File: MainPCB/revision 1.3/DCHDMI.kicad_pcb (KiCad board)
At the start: 4 copper layers, 66.6 x 51.3 mm, 105 parts, among them CON1 3-1775333-2, CON2 DC2R019JA7R1700, CON3 CONN_01X06, CON4 CONN_01X03, CON5 CONN_01X03, SW1 SW_DIP_x02, U1 MCP1826S-1202E/DB, U2 MIC5219-2.5YM5-TR, U3 LP5907MFX-1.8/NOPB, U4 ADV7513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

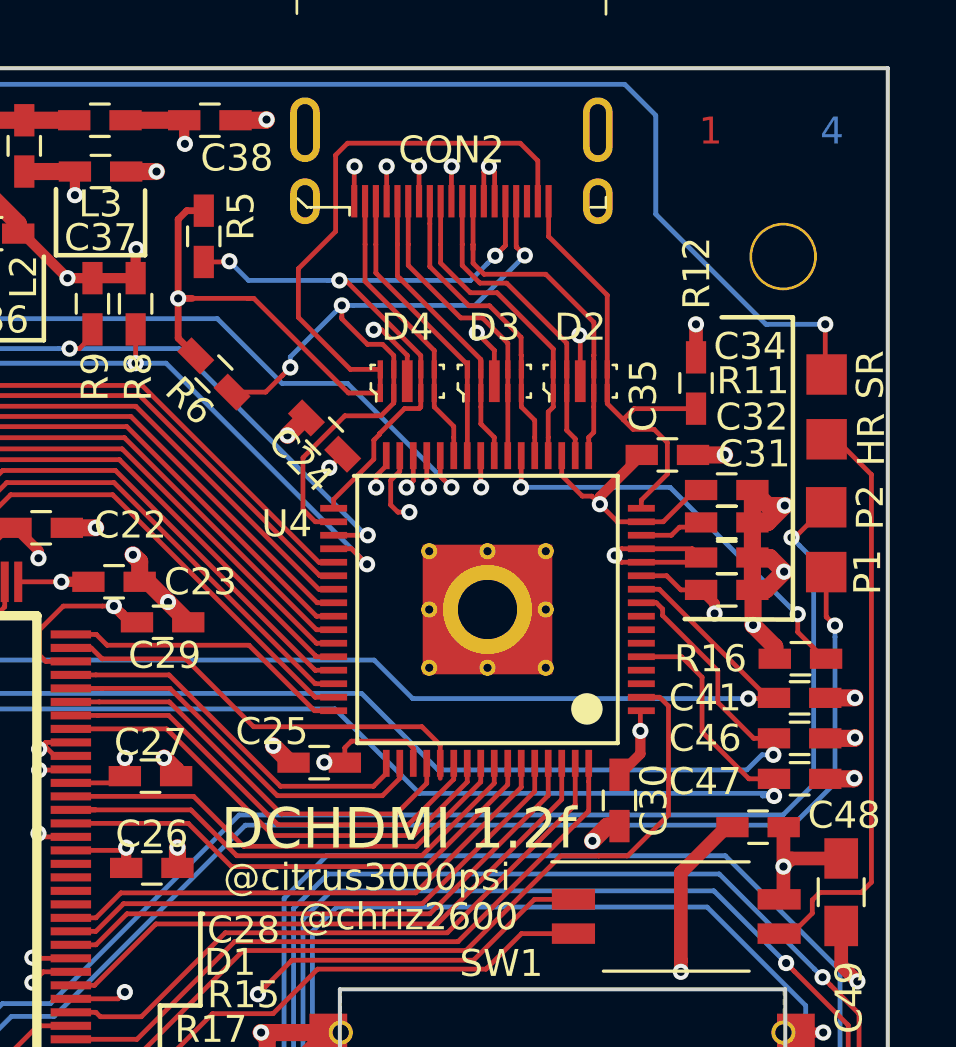
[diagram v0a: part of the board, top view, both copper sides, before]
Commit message: Added 470 series resistor
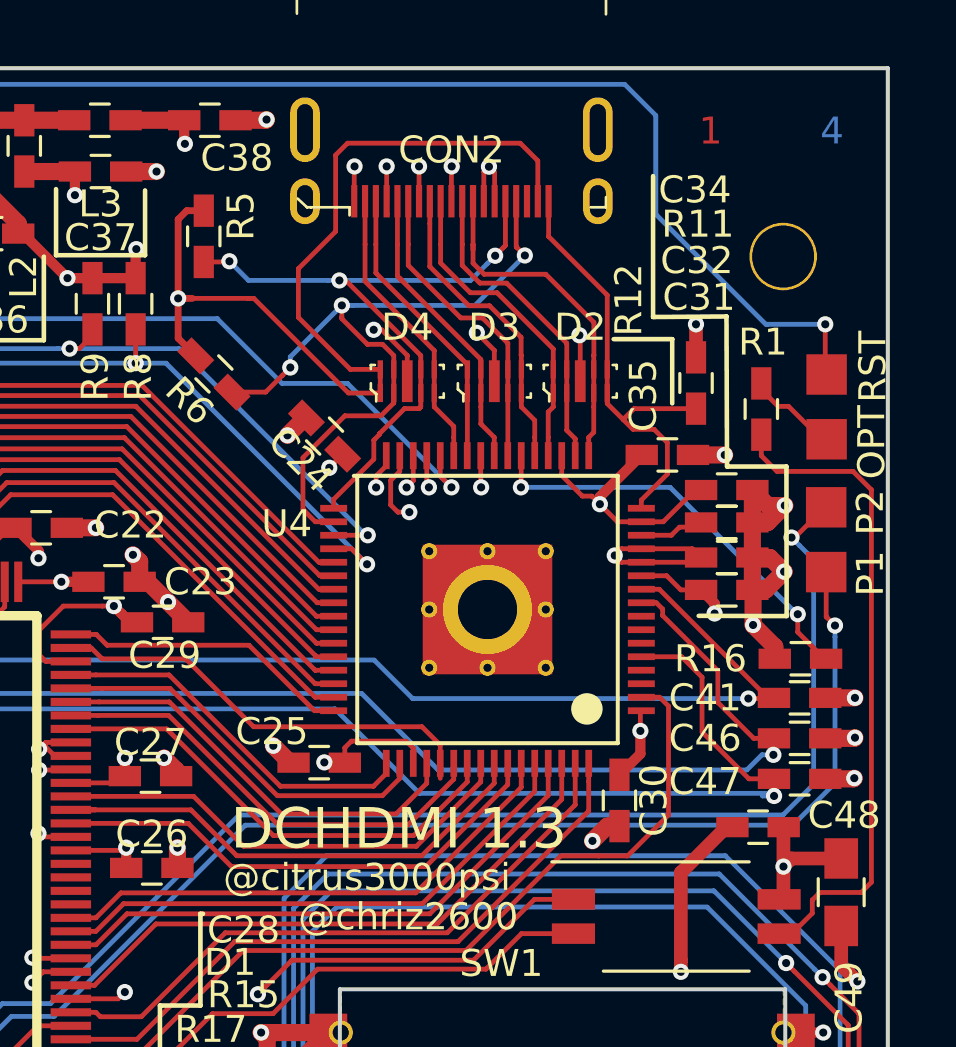
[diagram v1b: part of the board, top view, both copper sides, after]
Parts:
- added R1: 470, Capacitors_SMD:C_0603_HandSoldering, F.Cu at (183.9, 86.3)
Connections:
- SW1 pad 3: /HRST_OUT -> Net-(R1-Pad2)
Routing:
- net Net-(R1-Pad2): track 0.00 -> 24.8 mm
- net /HRST_OUT: track 22.2 -> 3.76 mm
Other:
- board text added: "DCHDMI 1.3"
- board text added: "OPT"
- board text added: "RST"
- board text removed: "DCHDMI 1.2f"
- board text removed: "HR"
- board text removed: "SR"
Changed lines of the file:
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@@
   (general
     (thickness 1.6)
-    (drawings 63)
-    (tracks 1976)
+    (drawings 68)
+    (tracks 1984)
     (zones 0)
-    (modules 105)
-    (nets 130)
+    (modules 106)
+    (nets 131)
   )
   (page A4)
@@
   (net 128 "Net-(U6-Pad22)")
   (net 129 "Net-(U8-Pad1)")
+  (net 130 "Net-(R1-Pad2)")
   (net_class Default "This is the default net class."
     (clearance 0.15)
@@
     (add_net "Net-(CON3-Pad6)")
     (add_net "Net-(D1-Pad1)")
+    (add_net "Net-(R1-Pad2)")
     (add_net "Net-(R11-Pad1)")
     (add_net "Net-(R14-Pad1)")
@@
     (tags "capacitor 0603")
     (attr smd)
-    (fp_text reference C31 (at 1.01 -5.04) (layer F.SilkS)
+    (fp_text reference C31 (at -1.03 -10.84) (layer F.SilkS)
       (effects (font (size 1 1) (thickness 0.15)))
     )
@@
       (effects (font (size 0.2 0.2) (thickness 0.05)))
     )
-    (fp_text user %R (at 1.01 -5.03) (layer F.Fab)
+    (fp_text user %R (at -1.03 -10.83) (layer F.Fab)
       (effects (font (size 1 1) (thickness 0.15)))
     )
@@
     (tags "capacitor 0603")
     (attr smd)
-    (fp_text reference C32 (at 0.93 -5.2) (layer F.SilkS)
+    (fp_text reference C32 (at -1.11 -11) (layer F.SilkS)
       (effects (font (size 1 1) (thickness 0.15)))
     )
@@
       (effects (font (size 0.2 0.2) (thickness 0.05)))
     )
-    (fp_text user %R (at 0.93 -5.22) (layer F.Fab)
+    (fp_text user %R (at -1.11 -11.02) (layer F.Fab)
       (effects (font (size 1 1) (thickness 0.15)))
     )
@@
     (tags "capacitor 0603")
     (attr smd)
-    (fp_text reference C34 (at 0.86 -5.32) (layer F.SilkS)
+    (fp_text reference C34 (at -1.18 -11.12) (layer F.SilkS)
       (effects (font (size 1 1) (thickness 0.15)))
     )
@@
       (effects (font (size 0.2 0.2) (thickness 0.05)))
     )
-    (fp_text user %R (at 0.89 -5.36) (layer F.Fab)
+    (fp_text user %R (at -1.15 -11.16) (layer F.Fab)
       (effects (font (size 1 1) (thickness 0.15)))
     )
@@
     (tags "capacitor 0603")
     (attr smd)
-    (fp_text reference R11 (at 0.97 -5.25) (layer F.SilkS)
+    (fp_text reference R11 (at -1.07 -11.05) (layer F.SilkS)
       (effects (font (size 1 1) (thickness 0.15)))
     )
@@
       (effects (font (size 0.2 0.2) (thickness 0.05)))
     )
-    (fp_text user %R (at 0.97 -5.25) (layer F.Fab)
+    (fp_text user %R (at -1.07 -11.05) (layer F.Fab)
       (effects (font (size 1 1) (thickness 0.15)))
     )
@@
     (tags "capacitor 0603")
     (attr smd)
-    (fp_text reference R12 (at 4.0648 0.0282 90) (layer F.SilkS)
+    (fp_text reference R12 (at 3.0748 -2.4918 270) (layer F.SilkS)
       (effects (font (size 1 1) (thickness 0.15)))
     )
@@
       (effects (font (size 0.2 0.2) (thickness 0.05)))
     )
-    (fp_text user %R (at 4.0948 0.0482 90) (layer F.Fab)
+    (fp_text user %R (at 3.0848 -2.5118 90) (layer F.Fab)
       (effects (font (size 1 1) (thickness 0.15)))
     )
@@
       (net 113 /ESP_SCL))
     (pad 3 smd rect (at 3.81 0.635) (size 1.6 0.76) (layers F.Cu F.Mask)
-      (net 122 /HRST_OUT))
+      (net 130 "Net-(R1-Pad2)"))
     (pad 2 smd rect (at -3.81 0.635) (size 1.6 0.76) (layers F.Cu F.Mask)
       (net 123 /HRST))
@@
     )
   )
-  (gr_line (start 185.05 94.1) (end 181.04 94.08) (layer F.SilkS) (width 0.17))
-  (gr_line (start 185.05 82.9) (end 185.05 94.1) (layer F.SilkS) (width 0.17))
-  (gr_line (start 182.41 82.9) (end 185.05 82.9) (layer F.SilkS) (width 0.17))
-  (gr_text SR (at 187.92 85.03 90) (layer F.SilkS)
+  (module Capacitors_SMD:C_0603_HandSoldering (layer F.Cu)
+    (at 183.88 86.3 270)
+    (descr "Capacitor SMD 0603, hand soldering")
+    (tags "capacitor 0603")
+    (attr smd)
+    (fp_text reference R1 (at -2.48 -0.06) (layer F.SilkS)
+      (effects (font (size 1 1) (thickness 0.15)))
+    )
+    (fp_text value 470 (at -0.01 0) (layer F.Fab)
+      (effects (font (size 0.15 0.15) (thickness 0.0375)))
+    )
+    (fp_text user %R (at -2.48 -0.04) (layer F.Fab)
+      (effects (font (size 1 1) (thickness 0.15)))
+    )
+    (fp_line (start -0.8 0.4) (end -0.8 -0.4) (layer F.Fab) (width 0.1))
+    (fp_line (start 0.8 0.4) (end -0.8 0.4) (layer F.Fab) (width 0.1))
+    (fp_line (start 0.8 -0.4) (end 0.8 0.4) (layer F.Fab) (width 0.1))
+    (fp_line (start -0.8 -0.4) (end 0.8 -0.4) (layer F.Fab) (width 0.1))
+    (fp_line (start -0.35 -0.6) (end 0.35 -0.6) (layer F.SilkS) (width 0.12))
+    (fp_line (start 0.35 0.6) (end -0.35 0.6) (layer F.SilkS) (width 0.12))
+    (fp_line (start -1.8 -0.65) (end 1.8 -0.65) (layer F.CrtYd) (width 0.05))
+    (fp_line (start -1.8 -0.65) (end -1.8 0.65) (layer F.CrtYd) (width 0.05))
+    (fp_line (start 1.8 0.65) (end 1.8 -0.65) (layer F.CrtYd) (width 0.05))
+    (fp_line (start 1.8 0.65) (end -1.8 0.65) (layer F.CrtYd) (width 0.05))
+    (pad 1 smd rect (at -0.95 0 270) (size 1.2 0.75) (layers F.Cu F.Paste F.Mask)
+      (net 122 /HRST_OUT))
+    (pad 2 smd rect (at 0.95 0 270) (size 1.2 0.75) (layers F.Cu F.Paste F.Mask)
+      (net 130 "Net-(R1-Pad2)"))
+    (model Capacitors_SMD.3dshapes/C_0603.wrl
+      (at (xyz 0 0 0))
+      (scale (xyz 1 1 1))
+      (rotate (xyz 0 0 0))
+    )
+  )
+  (gr_line (start 184.82 93.97) (end 181.56 93.96) (layer F.SilkS) (width 0.17))
+  (gr_line (start 184.81 88.43) (end 184.82 93.97) (layer F.SilkS) (width 0.17))
+  (gr_line (start 182.61 88.43) (end 184.81 88.43) (layer F.SilkS) (width 0.17))
+  (gr_line (start 182.59 82.87) (end 182.61 88.43) (layer F.SilkS) (width 0.17))
+  (gr_line (start 179.87 82.89) (end 182.59 82.87) (layer F.SilkS) (width 0.17))
+  (gr_line (start 179.87 77.67) (end 179.87 82.89) (layer F.SilkS) (width 0.17))
+  (gr_line (start 180.58 83.71) (end 180.58 86.09) (layer F.SilkS) (width 0.17))
+  (gr_line (start 178.41 83.71) (end 180.58 83.71) (layer F.SilkS) (width 0.17))
+  (gr_text RST (at 188.01 84.73 90) (layer F.SilkS)
     (effects (font (size 1 1) (thickness 0.15)))
   )
-  (gr_text HR (at 187.96 87.43 90) (layer F.SilkS)
+  (gr_text OPT (at 187.97 87.53 90) (layer F.SilkS)
     (effects (font (size 1 1) (thickness 0.15)))
   )
@@
   (gr_line (start 166.6 111.35) (end 166.6 112.4) (angle 90) (layer F.SilkS) (width 0.17))
   (gr_line (start 158.29 124.44) (end 165.55 124.44) (angle 90) (layer F.SilkS) (width 0.17))
-  (gr_text P2 (at 187.92 89.94 90) (layer F.SilkS)
+  (gr_text P2 (at 187.92 90.13 90) (layer F.SilkS)
     (effects (font (size 1 1) (thickness 0.15)))
   )
-  (gr_text P1 (at 187.82 92.34 90) (layer F.SilkS)
+  (gr_text P1 (at 187.92 92.39 90) (layer F.SilkS)
     (effects (font (size 1 1) (thickness 0.15)))
   )
@@
     (effects (font (size 1 1) (thickness 0.1)))
   )
-  (gr_text "DCHDMI 1.2f" (at 170.45 101.85) (layer F.SilkS)
+  (gr_text "DCHDMI 1.3" (at 170.45 101.85) (layer F.SilkS)
     (effects (font (size 1.5 1.5) (thickness 0.25)))
   )
@@
   (segment (start 178.82 74.27) (end 179.97 75.42) (width 0.178) (layer B.Cu) (net 121))
   (segment (start 141.94 84.57) (end 147.82 78.69) (width 0.178) (layer B.Cu) (net 121))
-  (segment (start 184.54 105.735) (end 184.12 105.735) (width 0.178) (layer F.Cu) (net 122))
-  (segment (start 187.96 88.73) (end 186.65 87.42) (width 0.178) (layer F.Cu) (net 122))
-  (segment (start 187.96 103.83) (end 187.96 88.73) (width 0.178) (layer F.Cu) (net 122))
-  (segment (start 185.015 105.735) (end 185.77 104.98) (width 0.178) (layer F.Cu) (net 122))
-  (segment (start 184.54 105.735) (end 185.015 105.735) (width 0.178) (layer F.Cu) (net 122))
-  (segment (start 185.77 104.98) (end 185.77 104.49) (width 0.178) (layer F.Cu) (net 122))
   (segment (start 186.65 87.42) (end 186.3 87.42) (width 0.178) (layer F.Cu) (net 122))
-  (segment (start 185.77 104.49) (end 186.05 104.21) (width 0.178) (layer F.Cu) (net 122))
-  (segment (start 186.05 104.21) (end 187.58 104.21) (width 0.178) (layer F.Cu) (net 122))
-  (segment (start 187.58 104.21) (end 187.96 103.83) (width 0.178) (layer F.Cu) (net 122))
+  (segment (start 186.11 87.42) (end 186.3 87.42) (width 0.178) (layer F.Cu) (net 122))
+  (segment (start 184.89 86.2) (end 186.11 87.42) (width 0.178) (layer F.Cu) (net 122))
+  (segment (start 184.505 86.2) (end 184.89 86.2) (width 0.178) (layer F.Cu) (net 122))
+  (segment (start 183.88 85.35) (end 183.88 85.575) (width 0.178) (layer F.Cu) (net 122))
+  (segment (start 183.88 85.575) (end 184.505 86.2) (width 0.178) (layer F.Cu) (net 122))
   (segment (start 157.754679 112.313199) (end 158.439599 112.313199) (width 0.178) (layer B.Cu) (net 123))
   (segment (start 157.217878 112.85) (end 157.754679 112.313199) (width 0.178) (layer B.Cu) (net 123))
@@
   (segment (start 149.914001 111.178001) (end 149.2 110.464) (width 0.178) (layer F.Cu) (net 128))
   (via (at 149.2 110.464) (size 0.6) (drill 0.3) (layers F.Cu B.Cu) (net 128))
+  (segment (start 184.54 105.735) (end 184.12 105.735) (width 0.178) (layer F.Cu) (net 130))
+  (segment (start 185.015 105.735) (end 185.77 104.98) (width 0.178) (layer F.Cu) (net 130))
+  (segment (start 184.54 105.735) (end 185.015 105.735) (width 0.178) (layer F.Cu) (net 130))
+  (segment (start 185.77 104.98) (end 185.77 104.49) (width 0.178) (layer F.Cu) (net 130))
+  (segment (start 185.77 104.49) (end 186.05 104.21) (width 0.178) (layer F.Cu) (net 130))
+  (segment (start 186.05 104.21) (end 187.58 104.21) (width 0.178) (layer F.Cu) (net 130))
+  (segment (start 187.58 104.21) (end 187.96 103.83) (width 0.178) (layer F.Cu) (net 130))
+  (segment (start 183.88 88.028) (end 184.462 88.61) (width 0.178) (layer F.Cu) (net 130))
+  (segment (start 183.88 87.25) (end 183.88 88.028) (width 0.178) (layer F.Cu) (net 130))
+  (segment (start 187.28 88.61) (end 187.96 89.29) (width 0.178) (layer F.Cu) (net 130))
+  (segment (start 184.462 88.61) (end 187.28 88.61) (width 0.178) (layer F.Cu) (net 130))
+  (segment (start 187.96 103.83) (end 187.96 89.29) (width 0.178) (layer F.Cu) (net 130))
   (zone (net 1) (net_name GND) (layer F.Cu) (hatch edge 0.508)
     (connect_pads (clearance 0.3))

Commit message: Fixed Issue
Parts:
- added R18: 470, Capacitors_SMD:C_0603_HandSoldering, F.Cu at (147.8, 82.0)
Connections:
- U6 pad 125: /SRST -> Net-(R18-Pad2)
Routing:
- net Net-(R18-Pad2): track 0.00 -> 57.3 mm, vias 0 -> 2
- net /SRST: track 109.3 -> 55.1 mm
- net /MISO: track 76.6 -> 77.2 mm
